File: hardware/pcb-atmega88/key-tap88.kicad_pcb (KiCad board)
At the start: 2 copper layers, 22 x 31 mm, 11 parts, among them J1 AVR-ISP-6x, J2 UART-CON-4, J3 CONN_01X08, J4 AMIGA-Keyboard-PINHEAD, J5 AMIGA-Keyboard-PINHEAD, U1 AtMega48PA

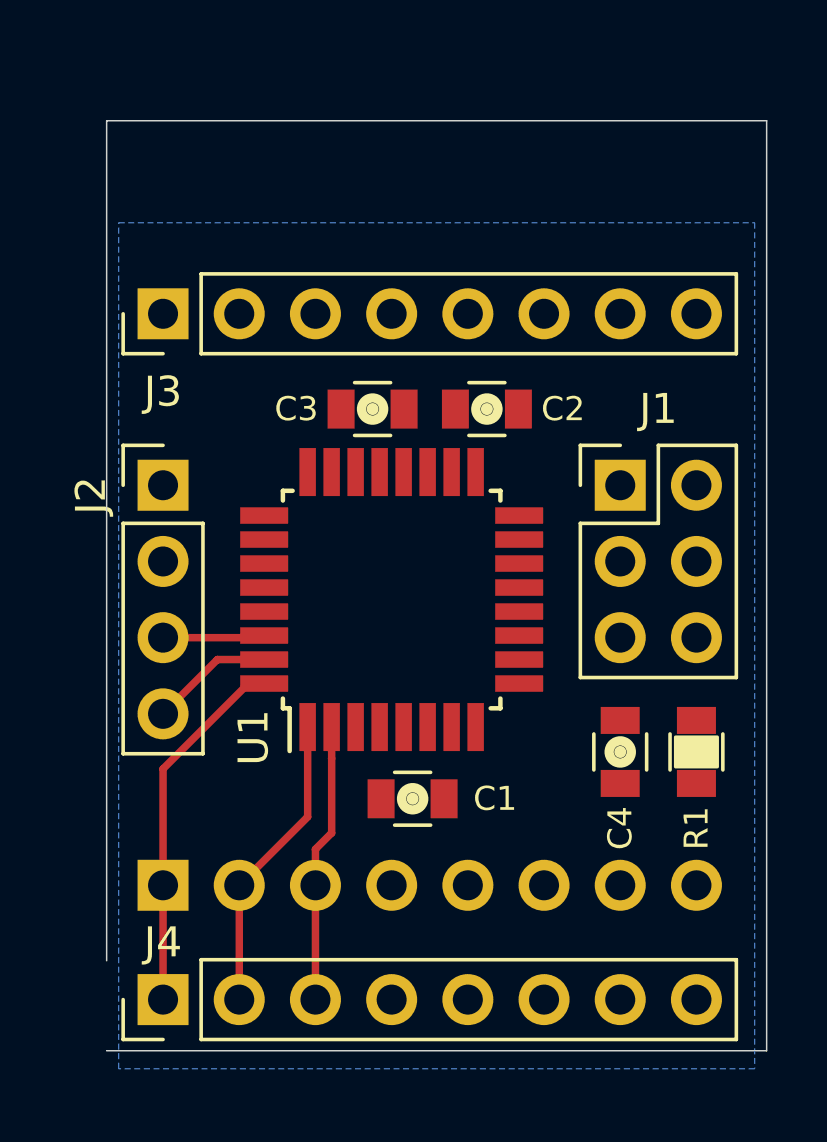
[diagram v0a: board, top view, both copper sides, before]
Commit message: * Added two solder Jumpers for Hardware configurability * Increased length of PCB tomake it sit on the DSUb connector in the back of an A500
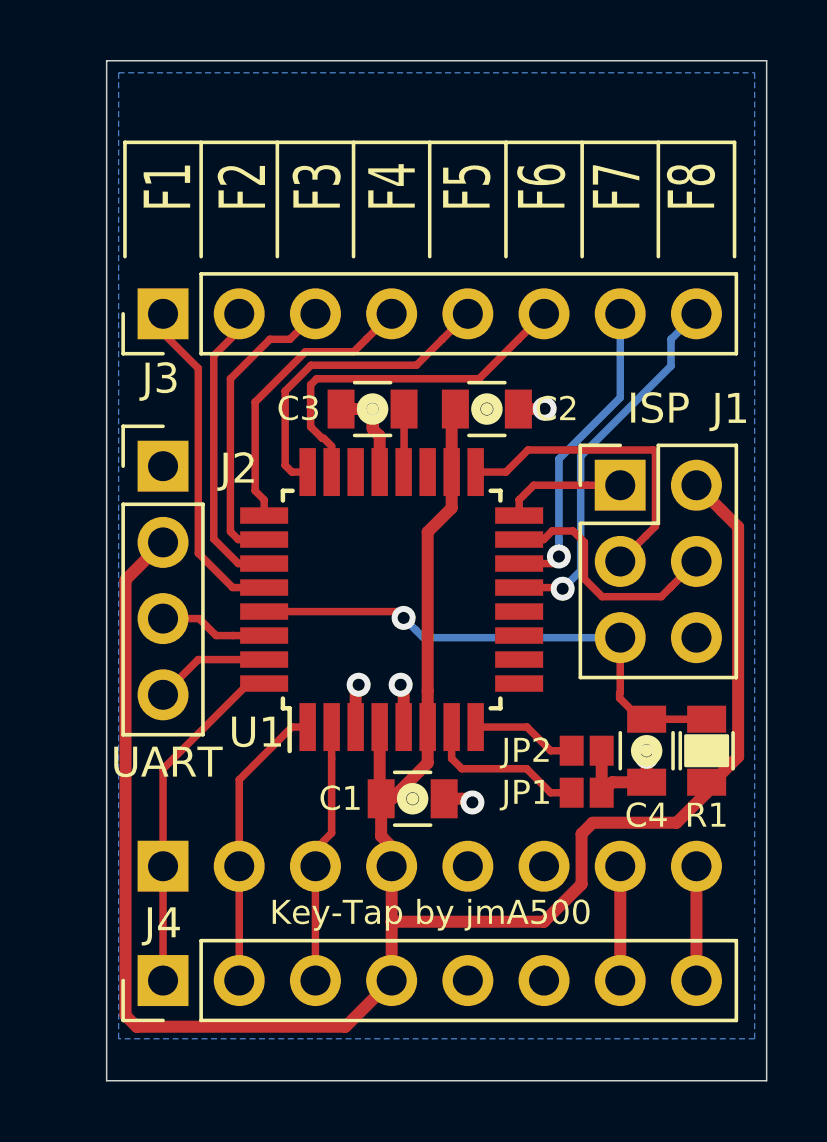
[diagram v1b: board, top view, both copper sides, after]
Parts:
- added JP1: SolderJumper_2_Open, Conn2:SMD-JUMPER, F.Cu at (70.0, 67.4)
- added JP2: SolderJumper_2_Open, Conn2:SMD-JUMPER, F.Cu at (70.0, 66.0)
- J5: footprint Pin_Headers:Pin_Header_Straight_1x08_Pitch2.54mm -> Socket_Strips:Socket_Strip_Straight_1x08_Pitch2.54mm
- moved C4 0.88 mm to (72.0, 66.0)
- moved J4 0.64 mm to (55.9, 73.7)
- moved J5 0.64 mm to (55.9, 69.8)
- moved J2 0.63 mm to (55.9, 56.5)
- moved R1 0.34 mm to (74.0, 66.0)
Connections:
- U1 pad 13: CF0 -> CF7
- U1 pad 14: CF1 -> CF6
- U1 pad 23: CF2 -> CF5
- U1 pad 24: CF3 -> CF4
- U1 pad 25: CF4 -> CF3
- U1 pad 26: CF5 -> CF2
- U1 pad 27: CF6 -> CF1
- U1 pad 28: CF7 -> CF0
- U1 pad 7: (no net) -> Net-(JP1-Pad2)
- U1 pad 8: (no net) -> Net-(JP2-Pad2)
- U1 pad 9: FLOPPY_LED -> (no net)
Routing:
- net +5V: track 0.00 -> 73.4 mm
- net /~RESET: track 0.00 -> 17.4 mm, vias 0 -> 1
- net CF7: track 0.00 -> 12.5 mm, vias 0 -> 1
- net CF5: track 0.00 -> 12.0 mm
- net GND: track 0.00 -> 11.9 mm, vias 0 -> 6
- net CF0: track 0.00 -> 11.2 mm
- net CF4: track 0.00 -> 10.5 mm
- net /SCK: track 0.00 -> 10.5 mm
- net CF6: track 0.00 -> 10.4 mm, vias 0 -> 1
- net CF2: track 0.00 -> 10.1 mm
- net CF1: track 0.00 -> 9.88 mm
- net CF3: track 0.00 -> 9.68 mm
- net /MOSI: track 0.00 -> 8.14 mm
- net Net-(JP1-Pad2): track 0.00 -> 5.52 mm
- net /MISO: track 0.00 -> 4.10 mm
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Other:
- board size 22 x 31 mm -> 22 x 34 mm
- board text added: "+5V"
- board text added: "F1 F2 F3 F4 F5 F6 F7 F8"
- board text added: "GND"
- board text added: "ISP"
- board text added: "Key-Tap by jmA500"
- board text added: "RxD"
- board text added: "TxD"
- board text added: "UART"
